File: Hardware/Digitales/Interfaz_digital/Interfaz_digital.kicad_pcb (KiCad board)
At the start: 2 copper layers, 115 x 90 mm, 47 parts, among them J0_1 Screw_Terminal_01x03, J0_2 Screw_Terminal_01x03, J0_3 Screw_Terminal_01x03, J1-1 Screw_Terminal_01x01, J1-2 Screw_Terminal_01x01, J2-1 Screw_Terminal_01x01, J2-2 Screw_Terminal_01x01, J3-1 Screw_Terminal_01x01, J3-2 Screw_Terminal_01x01, J4-1 Screw_Terminal_01x01, J4-2 Screw_Terminal_01x01, J5-1 Screw_Terminal_01x01, J5-2 Screw_Terminal_01x01, J6-1 Screw_Terminal_01x01, J6-2 Screw_Terminal_01x01, J7-1 Screw_Terminal_01x01, J7-2 Screw_Terminal_01x01, J8-1 Screw_Terminal_01x01, J8-2 Screw_Terminal_01x01, J9_1 Screw_Terminal_01x03, J9_2 Screw_Terminal_01x03, J9_3 Screw_Terminal_01x03, J9_4 Screw_Terminal_01x03, U1 TLP521-1, U2 TLP521-1, U3 TLP521-1, U4 TLP521-1, U5 TLP521-1, U6 TLP521-1, U7 TLP521-1, U8 TLP521-1

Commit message: Creación de PCB's con los archivos gerber y drill
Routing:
- net Net-(J0_1-Pin_1): track 0.00 -> 155.3 mm
- net Net-(J9_1-Pin_3): track 0.00 -> 118.6 mm
- net Net-(J9_1-Pin_2): track 0.00 -> 84.3 mm
- net Net-(J9_1-Pin_1): track 0.00 -> 40.4 mm
- net Net-(J9_4-Pin_3): track 0.00 -> 39.5 mm
- net Net-(J9_2-Pin_3): track 0.00 -> 37.7 mm
- net Net-(J9_3-Pin_1): track 0.00 -> 37.5 mm
- net Net-(J9_3-Pin_2): track 0.00 -> 35.8 mm
- net Net-(J9_2-Pin_2): track 0.00 -> 35.5 mm
- net Net-(J9_3-Pin_3): track 0.00 -> 34.5 mm
- net Net-(J9_2-Pin_1): track 0.00 -> 32.5 mm
- net Net-(J0_1-Pin_2): track 0.00 -> 29.8 mm
- net Net-(J0_3-Pin_3): track 0.00 -> 27.8 mm
- net Net-(J0_1-Pin_3): track 0.00 -> 23.3 mm
- net Net-(J0_3-Pin_2): track 0.00 -> 21.9 mm
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
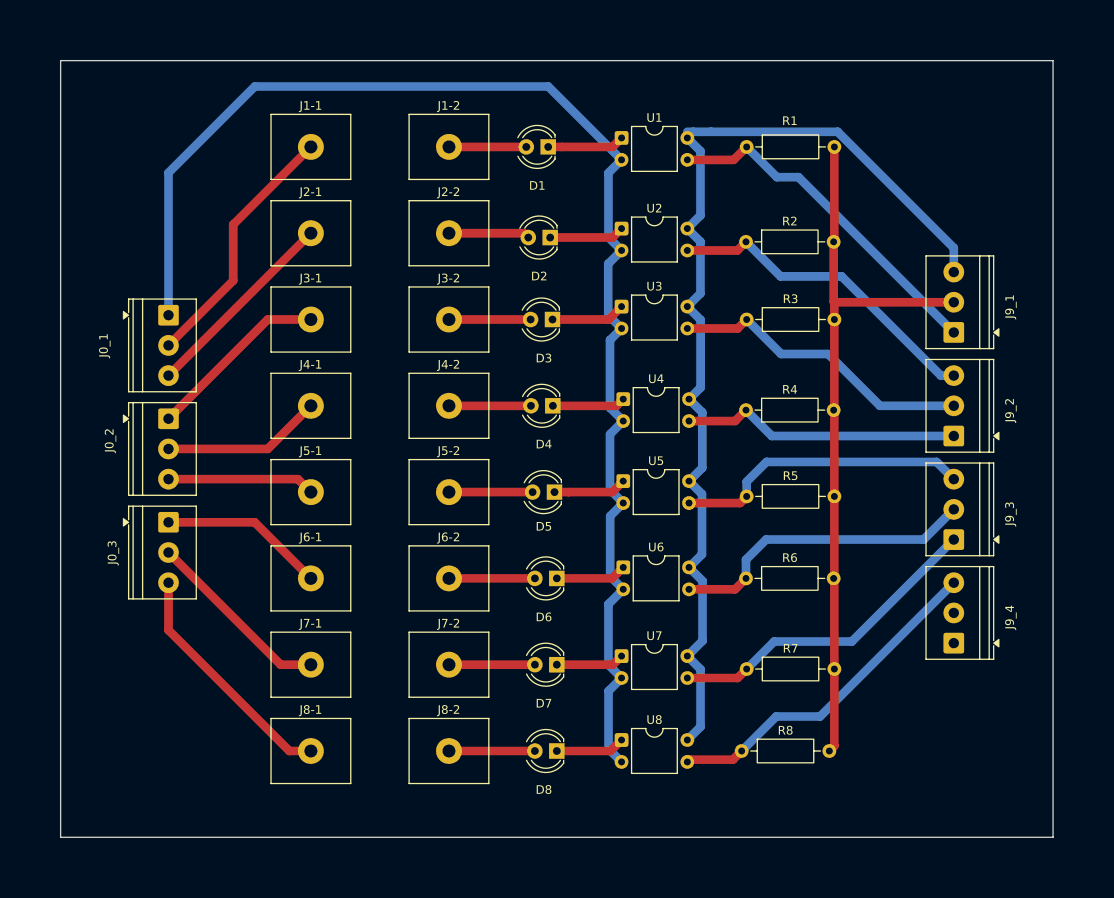
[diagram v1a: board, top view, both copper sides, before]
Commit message: Agregando agujeros para montaje a las PCB
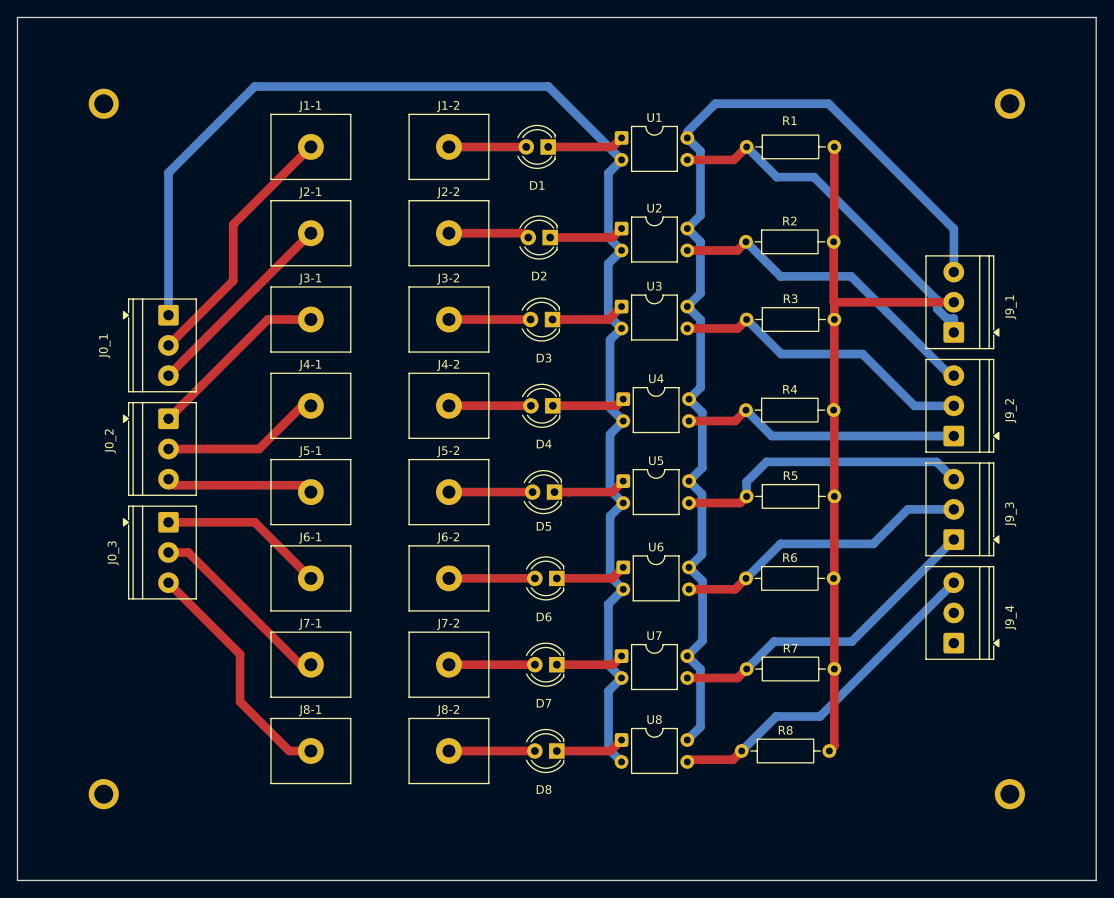
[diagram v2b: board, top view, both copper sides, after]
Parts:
- added REF**: MountingHole_2.2mm_M2_ISO7380_Pad, MountingHole:MountingHole_2.2mm_M2_ISO7380_Pad, F.Cu at (120.0, 130.0)
- added REF**: MountingHole_2.2mm_M2_ISO7380_Pad, MountingHole:MountingHole_2.2mm_M2_ISO7380_Pad, F.Cu at (225.0, 50.0)
- added REF**: MountingHole_2.2mm_M2_ISO7380_Pad, MountingHole:MountingHole_2.2mm_M2_ISO7380_Pad, F.Cu at (120.0, 50.0)
- added REF**: MountingHole_2.2mm_M2_ISO7380_Pad, MountingHole:MountingHole_2.2mm_M2_ISO7380_Pad, F.Cu at (225.0, 130.0)
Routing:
- net Net-(J9_1-Pin_3): track 118.6 -> 122.6 mm
- net Net-(J9_1-Pin_1): track 40.4 -> 41.9 mm
- net Net-(J9_3-Pin_2): track 35.8 -> 34.5 mm
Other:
- board size 115 x 90 mm -> 125 x 100 mm

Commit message: Ajustes a las interfaces digital y analogica
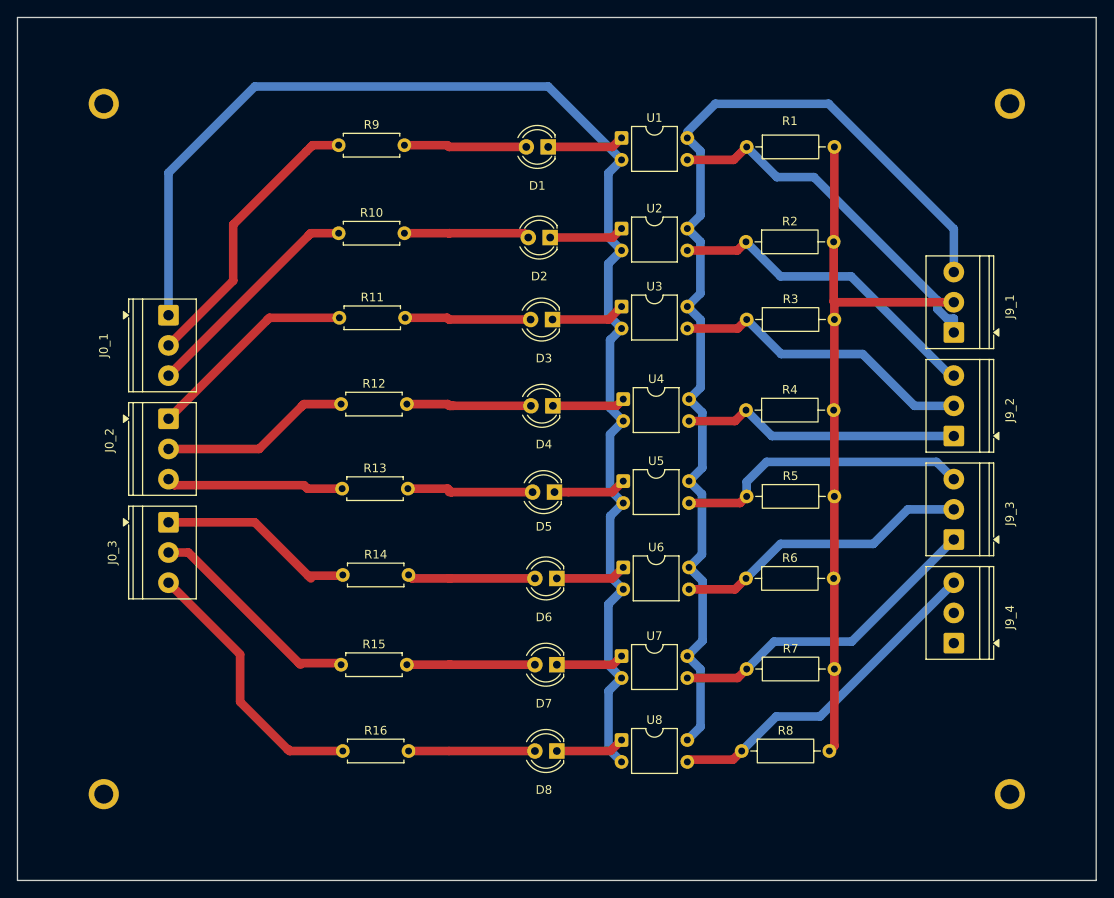
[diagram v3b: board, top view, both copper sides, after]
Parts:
- removed J1-1, J1-2, J2-1, J2-2, J3-1, J3-2, J4-1, J4-2, J5-1, J5-2, J6-1, J6-2, J7-1, J7-2, J8-1, J8-2: Screw_Terminal_01x01, TerminalBlock_MetzConnect:TerminalBlock_MetzConnect_360271_1x01_Horizontal_ScrewM3.0_Boxed
- added R10: R_US, Resistor_THT:R_Axial_DIN0207_L6.3mm_D2.5mm_P7.62mm_Horizontal, F.Cu at (147.2, 65.0)
- added R11: R_US, Resistor_THT:R_Axial_DIN0207_L6.3mm_D2.5mm_P7.62mm_Horizontal, F.Cu at (147.3, 74.8)
- added R12: R_US, Resistor_THT:R_Axial_DIN0207_L6.3mm_D2.5mm_P7.62mm_Horizontal, F.Cu at (147.5, 84.8)
- added R13: R_US, Resistor_THT:R_Axial_DIN0207_L6.3mm_D2.5mm_P7.62mm_Horizontal, F.Cu at (147.6, 94.6)
- added R14: R_US, Resistor_THT:R_Axial_DIN0207_L6.3mm_D2.5mm_P7.62mm_Horizontal, F.Cu at (147.7, 104.6)
- added R15: R_US, Resistor_THT:R_Axial_DIN0207_L6.3mm_D2.5mm_P7.62mm_Horizontal, F.Cu at (147.5, 115.0)
- added R16: R_US, Resistor_THT:R_Axial_DIN0207_L6.3mm_D2.5mm_P7.62mm_Horizontal, F.Cu at (147.7, 125.0)
- added R9: R_US, Resistor_THT:R_Axial_DIN0207_L6.3mm_D2.5mm_P7.62mm_Horizontal, F.Cu at (147.2, 54.8)
- renumbered REF** to H1, REF** to H2, REF** to H3, REF** to H4
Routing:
- net Net-(D4-A): track 9.50 -> 15.0 mm
- net Net-(D5-A): track 9.69 -> 15.0 mm
- net Net-(D2-A): track 9.40 -> 14.6 mm
- net Net-(D1-A): track 8.96 -> 14.2 mm
- net Net-(D3-A): track 9.46 -> 14.6 mm
- net Net-(D7-A): track 9.96 -> 15.0 mm
- net Net-(D6-A): track 9.96 -> 14.8 mm
- net Net-(D8-A): track 9.96 -> 14.6 mm
- net Net-(J0_3-Pin_1): track 19.2 -> 23.2 mm
- net Net-(J0_3-Pin_3): track 27.8 -> 31.8 mm
- net Net-(J0_3-Pin_2): track 21.9 -> 25.6 mm
- net Net-(J0_1-Pin_3): track 23.3 -> 27.0 mm
- net Net-(J0_2-Pin_2): track 18.6 -> 22.2 mm
- net Net-(J0_2-Pin_3): track 17.1 -> 20.6 mm
- net Net-(J0_2-Pin_1): track 21.3 -> 24.6 mm
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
